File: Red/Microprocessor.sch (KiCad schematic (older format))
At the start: 13 parts, among them IC201 STM32G473CET6, J201 Conn_01x06, SW201 SW_Push, U201 MAX7375AXR805, Y201 SIT1533AI-H4-DCC-32.768E

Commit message: Made one library in the project folder with all symbols and footprints for easy sharing
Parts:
- IC201: symbol SamacSys_Parts:STM32G473CET6 -> red_symbols:STM32G473CET6-SamacSys_Parts
- SW201: footprint my_library:SMD_Push_Switch -> Red:SMD_Push_Switch
- Y201: symbol SamacSys_Parts:SIT1533AI-H4-DCC-32.768E -> red_symbols:SIT1533AI-H4-DCC-32.768E-SamacSys_Parts
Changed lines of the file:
@@
 F 0 "SW201" V 4054 6898 50  0000 L CNN
 F 1 "SW_Push" V 4145 6898 50  0000 L CNN
-F 2 "my_library:SMD_Push_Switch" H 4100 6950 50  0001 C CNN
+F 2 "Red:SMD_Push_Switch" H 4100 6950 50  0001 C CNN
 F 3 "~" H 4100 6950 50  0001 C CNN
 F 4 "CKN9112CT-ND" V 4100 6750 50  0001 C CNN "digikey"
@@
 	4450 4450 4250 4450
 $Comp
-L SamacSys_Parts:STM32G473CET6 IC?
+L red_symbols:STM32G473CET6-SamacSys_Parts IC?
 U 1 1 5EBC4FB2
 P 4450 3350
@@
 32KHz
 $Comp
-L SamacSys_Parts:SIT1533AI-H4-DCC-32.768E Y201
+L red_symbols:SIT1533AI-H4-DCC-32.768E-SamacSys_Parts Y201
 U 1 1 5ECFA37E
 P 1200 4650
+AR Path="/5ECFA37E" Ref="Y201"  Part="1"
+AR Path="/5EC2F107/5ECFA37E" Ref="Y201"  Part="1"
 F 0 "Y201" H 1400 4200 50  0000 L CNN
 F 1 "SIT1533AI-H4-DCC-32.768E" H 650 4100 50  0000 L CNN

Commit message: Post design review
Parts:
- added TP701, TP702, TP703, TP704, TP705, TP706: TestPoint, Red:Test_Point_2.67x1.02mm, symbol Connector:TestPoint
- J701: renamed from J201; footprint Connector_PinHeader_2.54mm:PinHeader_1x06_P2.54mm_Vertical -> Red:j-link_6_pin_needle
- renumbered C201 to C701, C202 to C702, C208 to C703, C204 to C704, C205 to C705, C206 to C706, C209 to C707, IC201 to IC701, R201 to R701, SW201 to SW701, U201 to U701, Y201 to Y701
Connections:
- net labels added: INTERUPT, SWCLK, USART_CTS, USART_RTS
- net labels removed: D3, SWDCLK, USB_D+, USB_D-
- wire segments 84 -> 90
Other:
- note removed: "22 Ohm Resistors?\n"

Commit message: Swapped USBC connector out for one that was available, minor Silkscreen tweaks
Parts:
- C701: digikey 490-6326-2-ND -> 490-6326-1-ND
- C704, C705, C706, C707: digikey 490-6138-2-ND -> 490-5405-1-ND
- J701: digikey 732-5319-ND -> (none)
- R701: digikey PNM0603-50KBTR-ND -> 311-10KGRCT-ND
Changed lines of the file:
@@
 F 2 "Capacitor_SMD:C_0201_0603Metric" H 1788 800 50  0001 C CNN
 F 3 "~" H 1750 950 50  0001 C CNN
-F 4 "490-6138-2-ND" H 1750 950 50  0001 C CNN "digikey"
+F 4 "490-5405-1-ND" H 1750 950 50  0001 C CNN "digikey"
 	1    1750 950
 	1    0    0    -1
@@
 F 2 "Capacitor_SMD:C_0402_1005Metric" H 688 800 50  0001 C CNN
 F 3 "~" H 650 950 50  0001 C CNN
-F 4 "490-6326-2-ND" H 650 950 50  0001 C CNN "digikey"
+F 4 "490-6326-1-ND" H 650 950 50  0001 C CNN "digikey"
 	1    650  950
 	1    0    0    -1
@@
 F 2 "Capacitor_SMD:C_0201_0603Metric" H 2238 800 50  0001 C CNN
 F 3 "~" H 2200 950 50  0001 C CNN
-F 4 "490-6138-2-ND" H 2200 950 50  0001 C CNN "digikey"
+F 4 "490-5405-1-ND" H 2200 950 50  0001 C CNN "digikey"
 	1    2200 950
 	1    0    0    -1
@@
 F 2 "Capacitor_SMD:C_0201_0603Metric" H 2688 800 50  0001 C CNN
 F 3 "~" H 2650 950 50  0001 C CNN
-F 4 "490-6138-2-ND" H 2650 950 50  0001 C CNN "digikey"
+F 4 "490-5405-1-ND" H 2650 950 50  0001 C CNN "digikey"
 	1    2650 950
 	1    0    0    -1
@@
 F 2 "Capacitor_SMD:C_0201_0603Metric" H 3638 6600 50  0001 C CNN
 F 3 "~" H 3600 6750 50  0001 C CNN
-F 4 "490-6138-2-ND" H 3600 6750 50  0001 C CNN "digikey"
+F 4 "490-5405-1-ND" H 3600 6750 50  0001 C CNN "digikey"
 	1    3600 6750
 	1    0    0    -1
@@
 F 2 "Resistor_SMD:R_0603_1608Metric_Pad1.05x0.95mm_HandSolder" V 4030 6350 50  0001 C CNN
 F 3 "~" H 4100 6350 50  0001 C CNN
-F 4 "PNM0603-50KBTR-ND" H 4100 6350 50  0001 C CNN "digikey"
+F 4 "311-10KGRCT-ND" H 4100 6350 50  0001 C CNN "digikey"
 	1    4100 6350
 	1    0    0    -1
@@
 F 2 "Red:j-link_6_pin_needle" H 1750 6800 50  0001 C CNN
 F 3 "~" H 1750 6800 50  0001 C CNN
-F 4 "732-5319-ND" H 1750 6800 50  0001 C CNN "digikey"
+F 4 "" H 1750 6800 50  0001 C CNN "digikey"
 	1    1750 6800
 	-1   0    0    -1

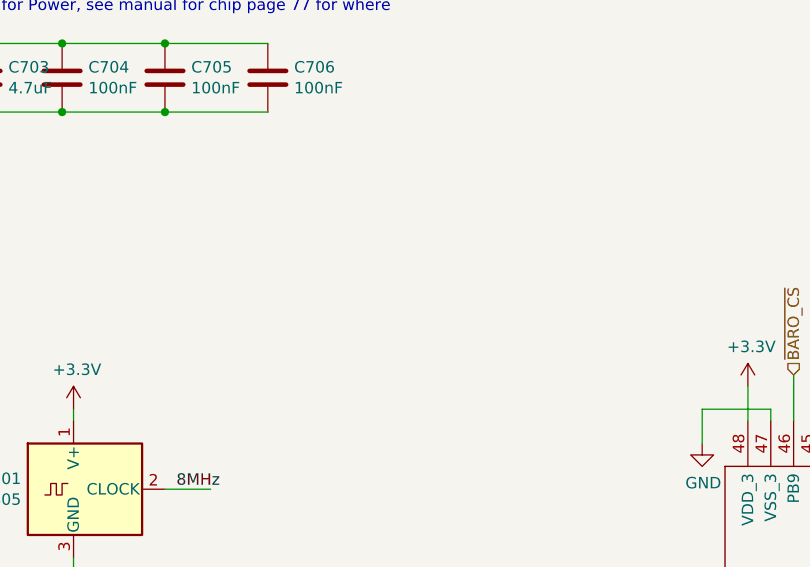
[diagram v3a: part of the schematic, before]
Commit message: Fixed a footprint error for the 32k clk
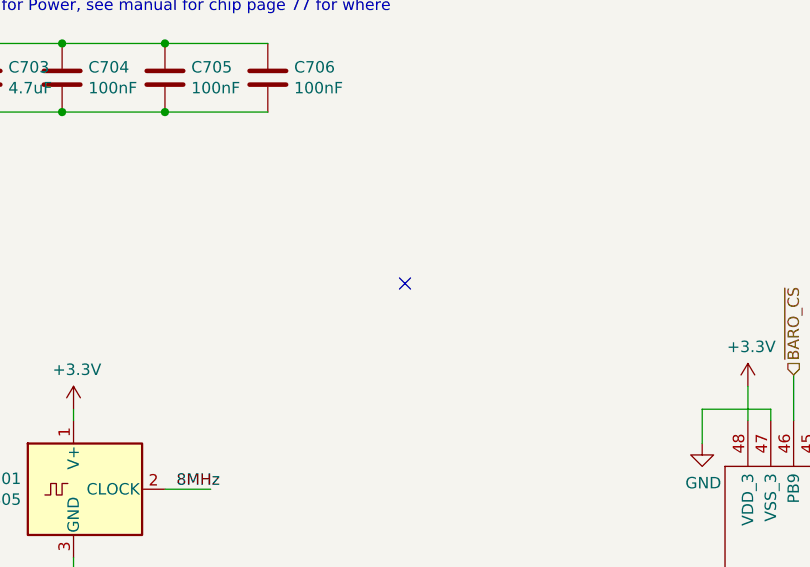
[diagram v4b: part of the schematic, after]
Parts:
- Y701: footprint SIT1533AIH4DCC32768E -> Red:SIT1533AIH4DCC32768E
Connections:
- no-connect marks 3 -> 4
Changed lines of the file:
@@
 F 0 "Y701" H 1400 4200 50  0000 L CNN
 F 1 "SIT1533AI-H4-DCC-32.768E" H 650 4100 50  0000 L CNN
-F 2 "SIT1533AIH4DCC32768E" H 2250 5050 50  0001 L CNN
+F 2 "Red:SIT1533AIH4DCC32768E" H 2250 5050 50  0001 L CNN
 F 3 "https://www.sitime.com/datasheet/SiT1533" H 2250 4950 50  0001 L CNN
 F 4 "Standard Clock Oscillators 32.768KHz R2R LVCMOS -40 to 85C 100ppm" H 2250 4850 50  0001 L CNN "Description"
@@
 Text Label 3350 4700 1    50   ~ 0
 QSPI_CLK
+NoConn ~ 3250 1850
 Wire Bus Line
 	4950 6000 6300 6000
